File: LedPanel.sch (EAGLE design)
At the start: 13 parts, among them U1 AL8805W5-7

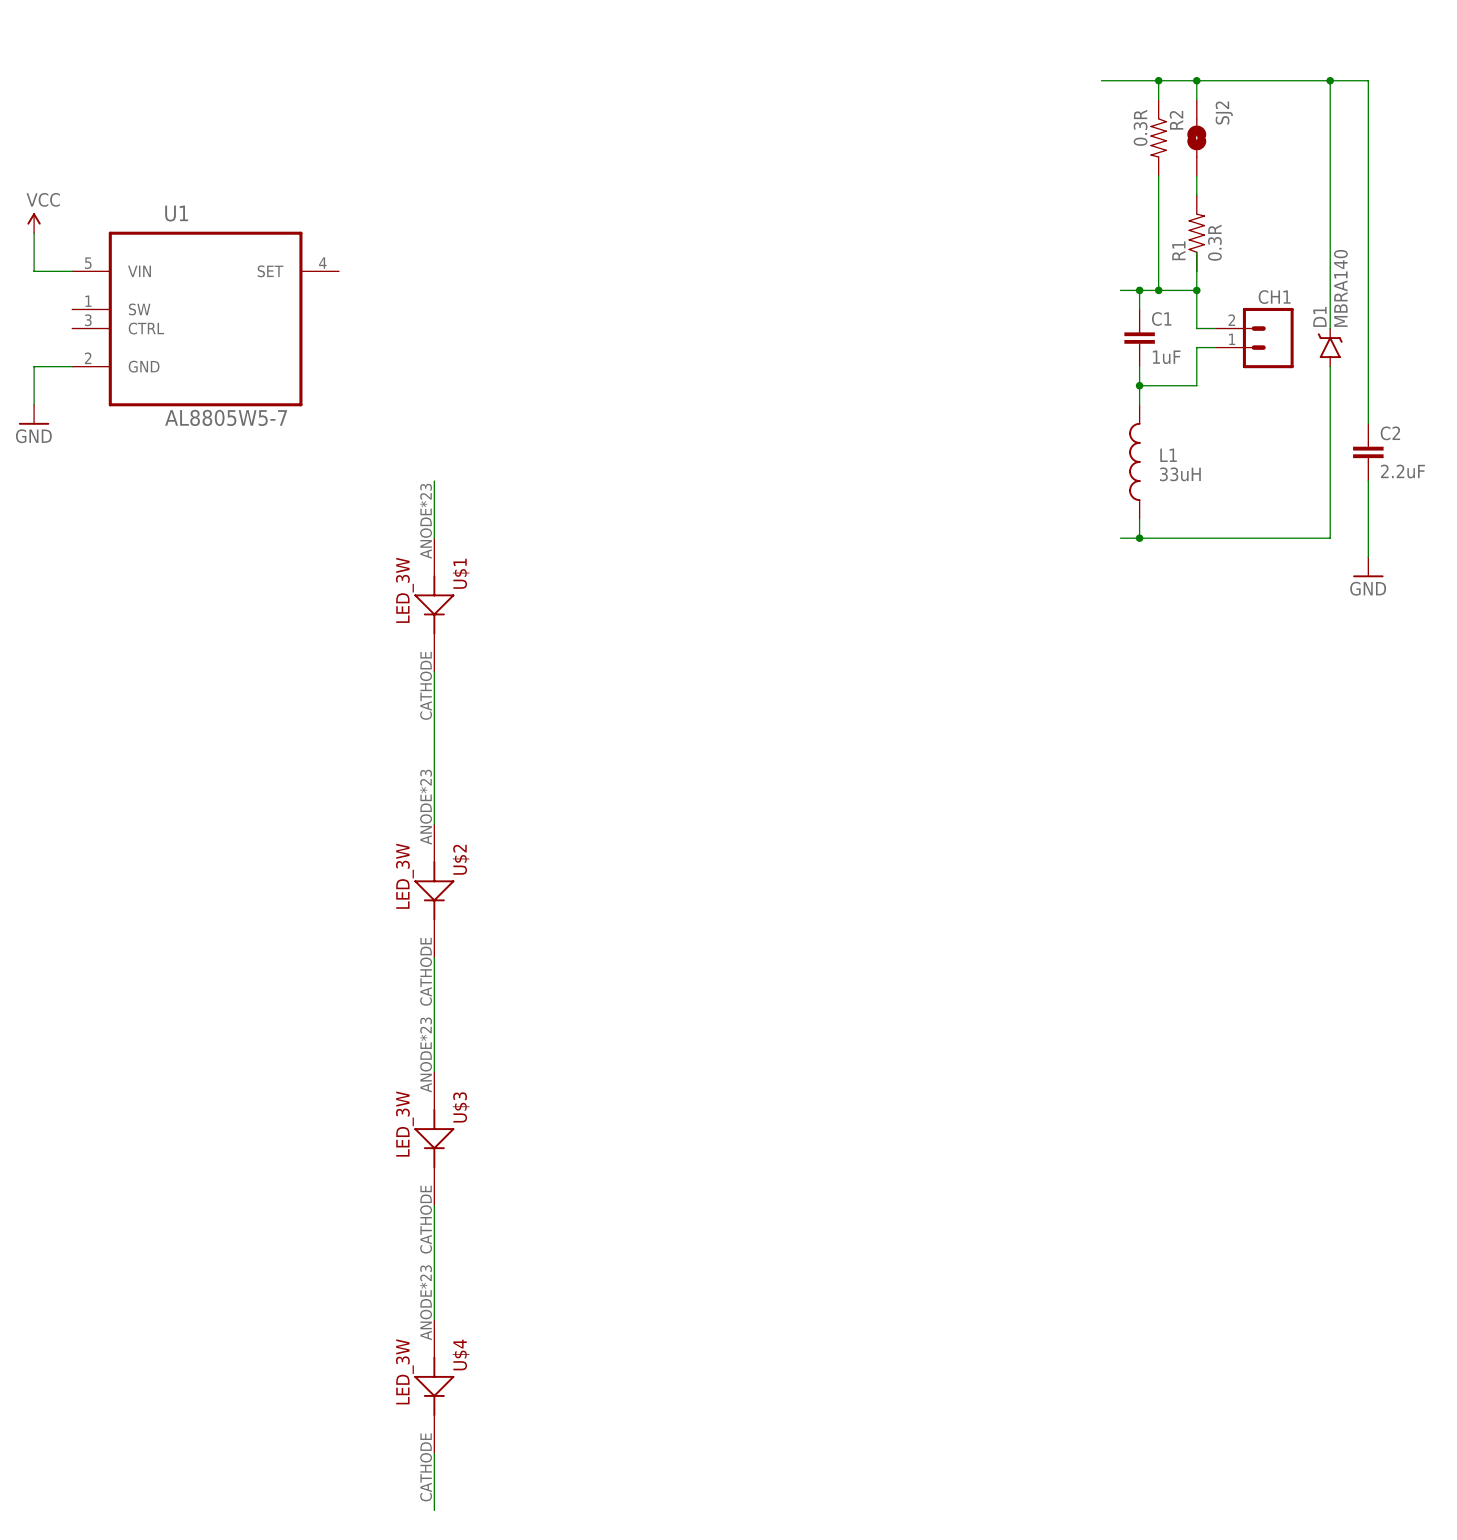
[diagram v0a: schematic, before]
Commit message: Connecting the led driver, fixing some issues
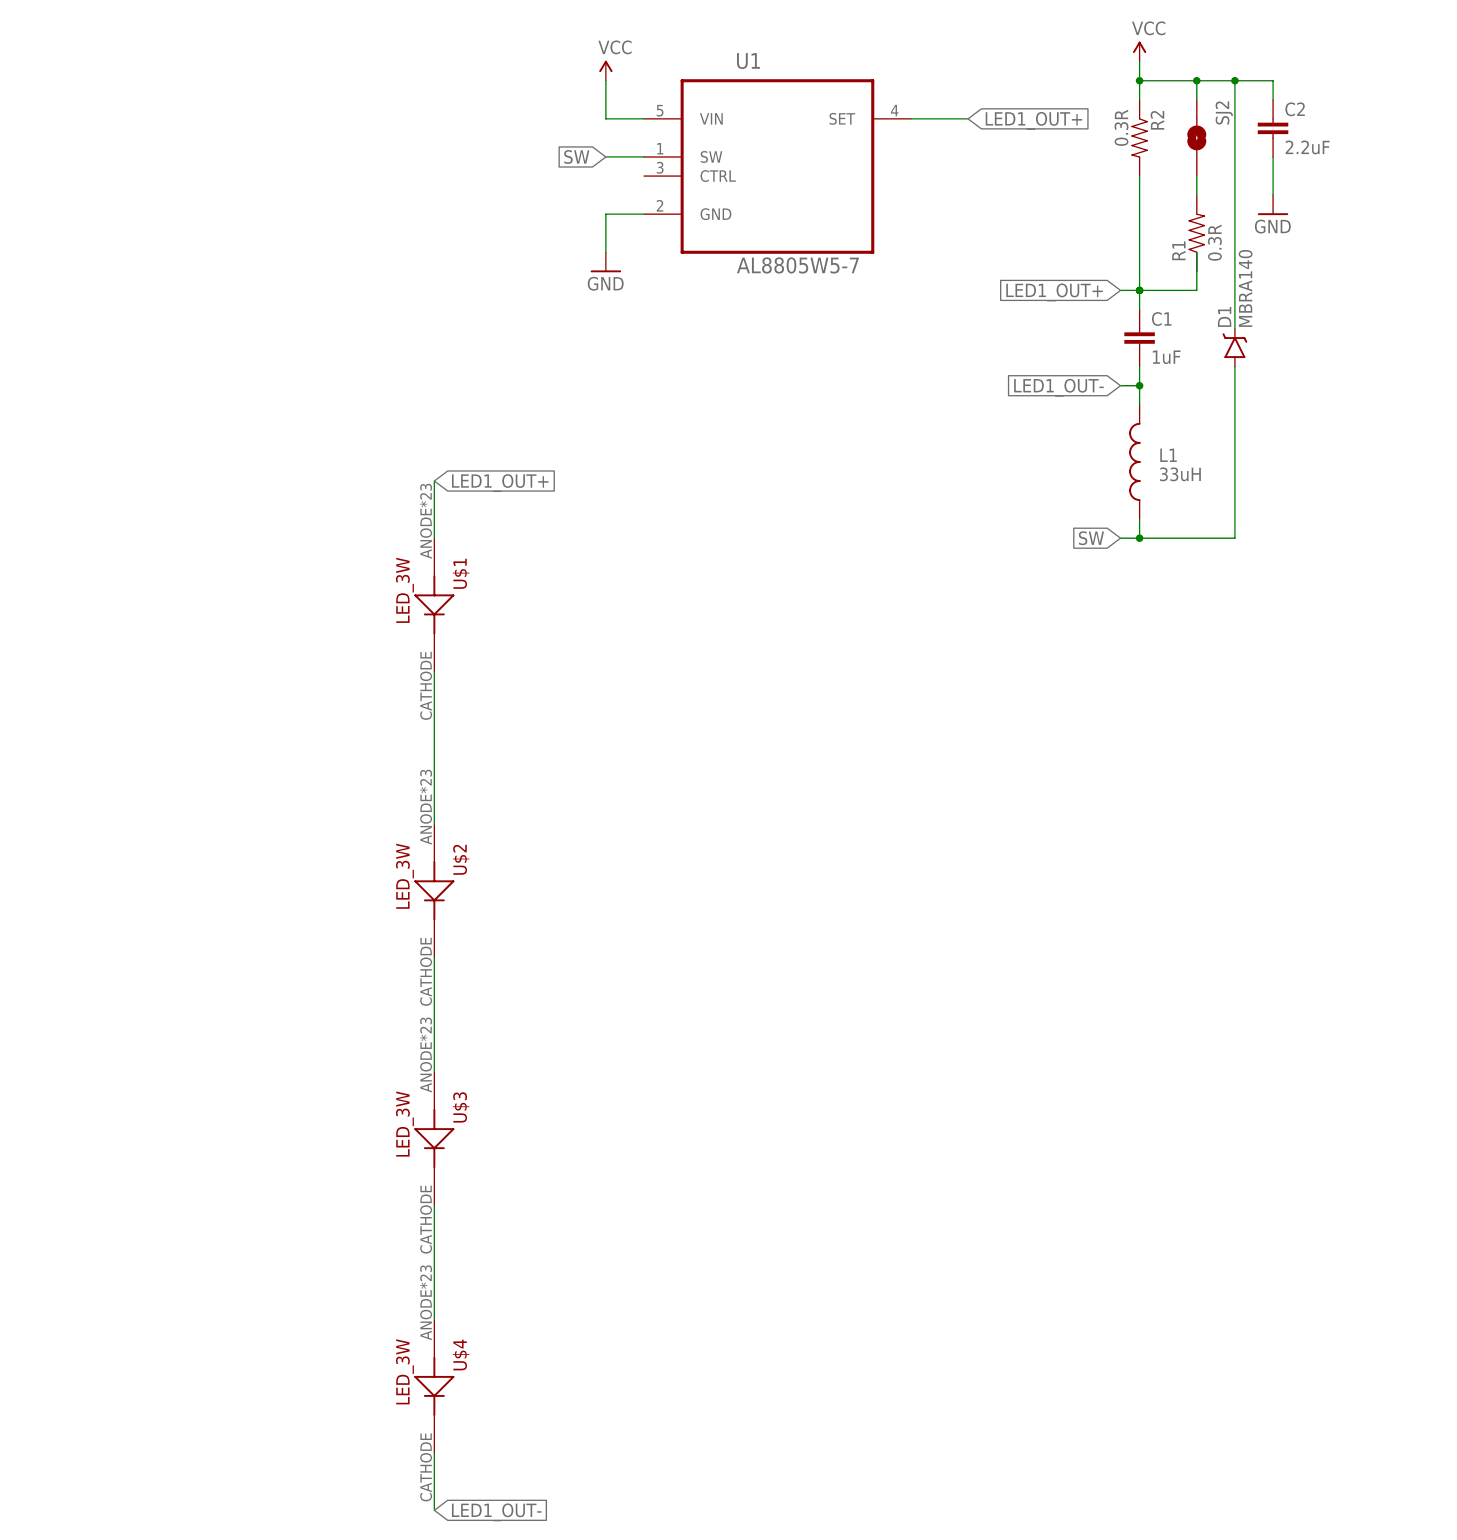
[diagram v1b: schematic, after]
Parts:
- removed CH1: (no value), SparkFun:M023.5MM_LOCK
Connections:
- removed net N$4: U$4.CATHODE
- removed net N$5: U$1.ANODE
- removed net OUT+: C1.1, CH1.2, R1.1, R2.2
- removed net OUT-: C1.2, CH1.1, L1.2
- removed net VIN: C2.1, D1.C, R2.1, SJ2.1
- new net LED1_OUT+: C1.1, R1.1, R2.2, U$1.ANODE, U1.SET
- new net LED1_OUT-: C1.2, L1.2, U$4.CATHODE
- net SW: now also U1.SW
- net VCC: now also C2.1, D1.C, R2.1, SJ2.1
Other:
- moved on the sheet: C2, D1, R2, U1
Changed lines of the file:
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@@
 <part name="GND13" library="SparkFun" deviceset="GND" device=""/>
 <part name="L1" library="SparkFun-Passives" deviceset="INDUCTOR" device="BOURNS_SRN6045" value="33uH"/>
-<part name="CH1" library="SparkFun" deviceset="M02" device="3.5MM_LOCK"/>
 <part name="D1" library="SparkFun-DiscreteSemi" deviceset="DIODE-SCHOTTKY" device="-MBRA140" value="MBRA140"/>
 <part name="R2" library="SparkFun-Resistors" deviceset="0.3OHM-1/8W-1%(0805)" device="" value="0.3R"/>
 <part name="SJ2" library="SparkFun-Passives" deviceset="JUMPER-PAD-2-NO" device="" value="NO Jumper"/>
+<part name="P+2" library="LedPanel" deviceset="VCC" device=""/>
 </parts>
 <sheets>
@@
 <instance part="U$3" gate="G$1" x="30.48" y="0" rot="R270"/>
 <instance part="U$4" gate="G$1" x="30.48" y="-33.02" rot="R270"/>
-<instance part="U1" gate="A" x="0" y="114.3"/>
-<instance part="P+1" gate="1" x="-22.86" y="121.92"/>
-<instance part="GND1" gate="1" x="-22.86" y="96.52"/>
+<instance part="U1" gate="A" x="76.2" y="134.62"/>
+<instance part="P+1" gate="1" x="53.34" y="142.24"/>
+<instance part="GND1" gate="1" x="53.34" y="116.84"/>
 <instance part="R1" gate="G$1" x="132.08" y="121.92" rot="R90"/>
 <instance part="C1" gate="G$1" x="124.46" y="106.68"/>
-<instance part="C2" gate="G$1" x="154.94" y="91.44"/>
-<instance part="GND13" gate="1" x="154.94" y="76.2"/>
+<instance part="C2" gate="G$1" x="142.24" y="134.62"/>
+<instance part="GND13" gate="1" x="142.24" y="124.46"/>
 <instance part="L1" gate="G$1" x="124.46" y="91.44" smashed="yes" rot="R180">
 <attribute name="NAME" x="127" y="91.44" size="1.778" layer="95"/>
 <attribute name="VALUE" x="127" y="88.9" size="1.778" layer="96"/>
 </instance>
-<instance part="CH1" gate="G$1" x="142.24" y="106.68" rot="MR0"/>
-<instance part="D1" gate="G$1" x="149.86" y="106.68" rot="R90"/>
-<instance part="R2" gate="G$1" x="127" y="134.62" rot="R270"/>
+<instance part="D1" gate="G$1" x="137.16" y="106.68" rot="R90"/>
+<instance part="R2" gate="G$1" x="124.46" y="134.62" rot="R270"/>
 <instance part="SJ2" gate="G$1" x="132.08" y="134.62" smashed="yes" rot="R270">
 <attribute name="NAME" x="134.62" y="139.7" size="1.778" layer="95" rot="R270"/>
 </instance>
+<instance part="P+2" gate="1" x="124.46" y="144.78"/>
 </instances>
 <busses>
@@
 </segment>
 </net>
-<net name="N$4" class="0">
-<segment>
-<pinref part="U$4" gate="G$1" pin="CATHODE"/>
-<wire x1="30.48" y1="-40.64" x2="30.48" y2="-48.26" width="0.1524" layer="91"/>
-</segment>
-</net>
-<net name="N$5" class="0">
+<net name="LED1_OUT+" class="0">
 <segment>
 <pinref part="U$1" gate="G$1" pin="ANODE"/>
 <wire x1="30.48" y1="81.28" x2="30.48" y2="88.9" width="0.1524" layer="91"/>
+<label x="30.48" y="88.9" size="1.778" layer="95" xref="yes"/>
+</segment>
+<segment>
+<pinref part="C1" gate="G$1" pin="1"/>
+<wire x1="124.46" y1="111.76" x2="124.46" y2="114.3" width="0.1524" layer="91"/>
+<wire x1="121.92" y1="114.3" x2="124.46" y2="114.3" width="0.1524" layer="91"/>
+<junction x="124.46" y="114.3"/>
+<wire x1="124.46" y1="114.3" x2="132.08" y2="114.3" width="0.1524" layer="91"/>
+<pinref part="R2" gate="G$1" pin="2"/>
+<wire x1="124.46" y1="129.54" x2="124.46" y2="114.3" width="0.1524" layer="91"/>
+<junction x="124.46" y="114.3"/>
+<wire x1="132.08" y1="114.3" x2="132.08" y2="116.84" width="0.1524" layer="91"/>
+<pinref part="R1" gate="G$1" pin="1"/>
+<wire x1="132.08" y1="119.38" x2="132.08" y2="116.84" width="0.1524" layer="91"/>
+<label x="121.92" y="114.3" size="1.778" layer="95" rot="R180" xref="yes"/>
+</segment>
+<segment>
+<pinref part="U1" gate="A" pin="SET"/>
+<wire x1="93.98" y1="137.16" x2="101.6" y2="137.16" width="0.1524" layer="91"/>
+<label x="101.6" y="137.16" size="1.778" layer="95" xref="yes"/>
 </segment>
 </net>
@@
 <segment>
 <pinref part="U1" gate="A" pin="VIN"/>
-<wire x1="-17.78" y1="116.84" x2="-22.86" y2="116.84" width="0.1524" layer="91"/>
+<wire x1="58.42" y1="137.16" x2="53.34" y2="137.16" width="0.1524" layer="91"/>
 <pinref part="P+1" gate="1" pin="VCC"/>
-<wire x1="-22.86" y1="116.84" x2="-22.86" y2="121.92" width="0.1524" layer="91"/>
+<wire x1="53.34" y1="137.16" x2="53.34" y2="142.24" width="0.1524" layer="91"/>
+</segment>
+<segment>
+<wire x1="137.16" y1="109.22" x2="137.16" y2="142.24" width="0.1524" layer="91"/>
+<pinref part="C2" gate="G$1" pin="1"/>
+<wire x1="137.16" y1="142.24" x2="142.24" y2="142.24" width="0.1524" layer="91"/>
+<wire x1="142.24" y1="142.24" x2="142.24" y2="139.7" width="0.1524" layer="91"/>
+<wire x1="124.46" y1="144.78" x2="124.46" y2="142.24" width="0.1524" layer="91"/>
+<wire x1="124.46" y1="142.24" x2="132.08" y2="142.24" width="0.1524" layer="91"/>
+<wire x1="132.08" y1="142.24" x2="137.16" y2="142.24" width="0.1524" layer="91"/>
+<junction x="137.16" y="142.24"/>
+<pinref part="D1" gate="G$1" pin="C"/>
+<pinref part="R2" gate="G$1" pin="1"/>
+<wire x1="124.46" y1="139.7" x2="124.46" y2="142.24" width="0.1524" layer="91"/>
+<junction x="124.46" y="142.24"/>
+<pinref part="SJ2" gate="G$1" pin="1"/>
+<wire x1="132.08" y1="139.7" x2="132.08" y2="142.24" width="0.1524" layer="91"/>
+<junction x="132.08" y="142.24"/>
+<pinref part="P+2" gate="1" pin="VCC"/>
 </segment>
 </net>
@@
 <pinref part="U1" gate="A" pin="GND"/>
 <pinref part="GND1" gate="1" pin="GND"/>
-<wire x1="-17.78" y1="104.14" x2="-22.86" y2="104.14" width="0.1524" layer="91"/>
-<wire x1="-22.86" y1="104.14" x2="-22.86" y2="99.06" width="0.1524" layer="91"/>
+<wire x1="58.42" y1="124.46" x2="53.34" y2="124.46" width="0.1524" layer="91"/>
+<wire x1="53.34" y1="124.46" x2="53.34" y2="119.38" width="0.1524" layer="91"/>
 </segment>
 <segment>
 <pinref part="C2" gate="G$1" pin="2"/>
-<wire x1="154.94" y1="88.9" x2="154.94" y2="78.74" width="0.1524" layer="91"/>
+<wire x1="142.24" y1="132.08" x2="142.24" y2="127" width="0.1524" layer="91"/>
 <pinref part="GND13" gate="1" pin="GND"/>
 </segment>
 </net>
-<net name="VIN" class="0">
-<segment>
-<wire x1="149.86" y1="109.22" x2="149.86" y2="142.24" width="0.1524" layer="91"/>
-<pinref part="C2" gate="G$1" pin="1"/>
-<wire x1="149.86" y1="142.24" x2="154.94" y2="142.24" width="0.1524" layer="91"/>
-<wire x1="154.94" y1="142.24" x2="154.94" y2="96.52" width="0.1524" layer="91"/>
-<wire x1="119.38" y1="142.24" x2="127" y2="142.24" width="0.1524" layer="91"/>
-<wire x1="127" y1="142.24" x2="132.08" y2="142.24" width="0.1524" layer="91"/>
-<wire x1="132.08" y1="142.24" x2="149.86" y2="142.24" width="0.1524" layer="91"/>
-<junction x="149.86" y="142.24"/>
-<pinref part="D1" gate="G$1" pin="C"/>
-<pinref part="R2" gate="G$1" pin="1"/>
-<wire x1="127" y1="139.7" x2="127" y2="142.24" width="0.1524" layer="91"/>
-<junction x="127" y="142.24"/>
-<pinref part="SJ2" gate="G$1" pin="1"/>
-<wire x1="132.08" y1="139.7" x2="132.08" y2="142.24" width="0.1524" layer="91"/>
-<junction x="132.08" y="142.24"/>
-</segment>
-</net>
-<net name="OUT-" class="1">
+<net name="LED1_OUT-" class="1">
 <segment>
 <pinref part="C1" gate="G$1" pin="2"/>
@@
 <junction x="124.46" y="101.6"/>
 <pinref part="L1" gate="G$1" pin="2"/>
-<wire x1="132.08" y1="101.6" x2="124.46" y2="101.6" width="0.1524" layer="91"/>
-<wire x1="132.08" y1="101.6" x2="132.08" y2="106.68" width="0.1524" layer="91"/>
-<pinref part="CH1" gate="G$1" pin="1"/>
-<wire x1="132.08" y1="106.68" x2="134.62" y2="106.68" width="0.1524" layer="91"/>
+<wire x1="124.46" y1="101.6" x2="121.92" y2="101.6" width="0.1524" layer="91"/>
+<label x="121.92" y="101.6" size="1.778" layer="95" rot="R180" xref="yes"/>
 </segment>
-</net>
-<net name="OUT+" class="0">
 <segment>
-<pinref part="C1" gate="G$1" pin="1"/>
-<wire x1="124.46" y1="111.76" x2="124.46" y2="114.3" width="0.1524" layer="91"/>
-<wire x1="121.92" y1="114.3" x2="124.46" y2="114.3" width="0.1524" layer="91"/>
-<junction x="124.46" y="114.3"/>
-<wire x1="124.46" y1="114.3" x2="127" y2="114.3" width="0.1524" layer="91"/>
-<wire x1="127" y1="114.3" x2="132.08" y2="114.3" width="0.1524" layer="91"/>
-<wire x1="132.08" y1="114.3" x2="132.08" y2="109.22" width="0.1524" layer="91"/>
-<pinref part="CH1" gate="G$1" pin="2"/>
-<wire x1="132.08" y1="109.22" x2="134.62" y2="109.22" width="0.1524" layer="91"/>
-<pinref part="R2" gate="G$1" pin="2"/>
-<wire x1="127" y1="129.54" x2="127" y2="114.3" width="0.1524" layer="91"/>
-<junction x="127" y="114.3"/>
-<wire x1="132.08" y1="114.3" x2="132.08" y2="116.84" width="0.1524" layer="91"/>
-<junction x="132.08" y="114.3"/>
-<pinref part="R1" gate="G$1" pin="1"/>
-<wire x1="132.08" y1="119.38" x2="132.08" y2="116.84" width="0.1524" layer="91"/>
+<pinref part="U$4" gate="G$1" pin="CATHODE"/>
+<wire x1="30.48" y1="-40.64" x2="30.48" y2="-48.26" width="0.1524" layer="91"/>
+<label x="30.48" y="-48.26" size="1.778" layer="95" xref="yes"/>
 </segment>
 </net>
@@
 <wire x1="121.92" y1="81.28" x2="124.46" y2="81.28" width="0.1524" layer="91"/>
 <wire x1="124.46" y1="81.28" x2="124.46" y2="83.82" width="0.1524" layer="91"/>
-<wire x1="149.86" y1="81.28" x2="149.86" y2="104.14" width="0.1524" layer="91"/>
-<wire x1="124.46" y1="81.28" x2="149.86" y2="81.28" width="0.1524" layer="91"/>
+<wire x1="137.16" y1="81.28" x2="137.16" y2="104.14" width="0.1524" layer="91"/>
+<wire x1="124.46" y1="81.28" x2="137.16" y2="81.28" width="0.1524" layer="91"/>
 <junction x="124.46" y="81.28"/>
 <pinref part="L1" gate="G$1" pin="1"/>
 <pinref part="D1" gate="G$1" pin="A"/>
+<label x="121.92" y="81.28" size="1.778" layer="95" rot="R180" xref="yes"/>
+</segment>
+<segment>
+<pinref part="U1" gate="A" pin="SW"/>
+<wire x1="58.42" y1="132.08" x2="53.34" y2="132.08" width="0.1524" layer="91"/>
+<label x="53.34" y="132.08" size="1.778" layer="95" rot="R180" xref="yes"/>
 </segment>
 </net>
